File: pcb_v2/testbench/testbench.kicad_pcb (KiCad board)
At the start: 2 copper layers, 274.3 x 124.5 mm, 70 parts, among them J1 test_A, J10 test_C1, J11 test_C2, J12 test_C3, J15 lcd, J17 DEBUG, J18 power_jack, J2 test_B, J3 sub_0, J4 sub_8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

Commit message: projeto enviado para impressao em dezembro/25
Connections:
- J10 pad 1: test_0 -> test_power_vcc
- J10 pad 10: test_power_gnd_C -> test_28
- J10 pad 12: test_power_gnd_C -> test_29
- J10 pad 14: test_power_gnd_C -> test_30
- J10 pad 15: test_7 -> test_power_gnd_C
- J10 pad 4: test_power_vcc -> test_25
- J10 pad 6: test_power_vcc -> test_26
- J10 pad 8: test_power_vcc -> test_27
- J9 pad 3: unconnected-(J9-Pin_3-Pad3) -> +5V
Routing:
- net test_7: track 106.3 -> 92.8 mm
- net test_0: track 102.4 -> 88.9 mm
- net test_26: track 105.8 -> 116.7 mm
- net test_30: track 109.9 -> 120.8 mm
- net test_29: track 109.2 -> 120.1 mm
- net test_28: track 108.0 -> 119.0 mm
- net test_25: track 104.7 -> 115.7 mm
- net test_27: track 106.9 -> 117.8 mm
- net +5V: track 581.1 -> 589.7 mm
- net test_power_vcc: track 281.5 -> 276.4 mm
- net test_power_gnd_C: track 123.6 -> 125.6 mm
- net test_33: track 79.1 -> 78.0 mm
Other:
- outline, holes or cut-outs redrawn
- board text added: "ALE"
- board text added: "GND"
- board text added: "IN+"
- board text added: "IN-"
- board text added: "RX"
- board text added: "SCL"
- board text added: "SDA"
- board text added: "TX"
- board text added: "VBS"
- board text added: "VCC"

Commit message: adicionados imagens 3D para os componentes customizados
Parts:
- moved SW5 0.19 mm to (32.6, 76.2)

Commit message: versao B2 da testbench (com a alimentacao das placas de teste reposicionadas para as extremidades
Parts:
- moved R5 42.0 mm to (219.7, 51.4)
- moved R1 31.1 mm to (219.7, 47.0)
- moved R15 29.4 mm to (227.3, 129.5)
- moved R14 28.9 mm to (237.5, 129.5)
- moved R13 27.3 mm to (232.4, 129.5)
- moved R3 21.9 mm to (219.7, 42.5)
- moved D6 6.35 mm to (247.7, 135.3)
- moved D5 3.18 mm to (257.8, 135.3)
- moved R2 2.84 mm to (256.5, 51.4)
- moved R4 2.84 mm to (245.1, 51.4)
- moved R6 2.84 mm to (268.0, 51.4)
- moved Q1 2.54 mm to (250.2, 47.0)
- moved Q2 2.54 mm to (238.8, 47.0)
- moved Q3 2.54 mm to (261.6, 47.0)
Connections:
- J1 pad 1: test_0 -> test_power_vcc
- J1 pad 10: test_power_gnd_A -> test_9
- J1 pad 14: test_13 -> test_power_gnd_A
- J1 pad 15: test_24 -> test_power_vcc
- J1 pad 23: test_power_vcc -> test_32
- J1 pad 24: test_power_gnd_A -> test_33
- J1 pad 28: test_37 -> test_power_gnd_A
- J1 pad 9: test_power_vcc -> test_8
- J2 pad 1: test_0 -> test_power_vcc
- J2 pad 22: test_21 -> test_power_gnd_B
- J2 pad 23: test_24 -> test_power_vcc
- J2 pad 30: test_power_vcc -> test_31
- J2 pad 31: test_power_gnd_B -> test_32
- J2 pad 44: test_45 -> test_power_gnd_B
- J2 pad 8: test_power_vcc -> test_7
- J2 pad 9: test_power_gnd_B -> test_8
- J9 pad 5: mcu_power_scl -> mcu_power_sda
- J9 pad 6: mcu_power_sda -> mcu_power_scl
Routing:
- net test_24: track 103.5 -> 0.00 mm, vias 2 -> 0
- net test_0: track 88.9 -> 0.00 mm, vias 1 -> 0
- net mcu_power_on_C: track 116.9 -> 75.1 mm
- net test_power_vcc: track 276.4 -> 236.2 mm, vias 2 -> 0
- net Net-(D6-A): track 47.0 -> 8.41 mm
- net test_power_gnd_A: track 149.7 -> 113.9 mm
- net Net-(Q3-G): track 13.9 -> 41.2 mm
- net mcu_power_on_A: track 109.3 -> 83.3 mm
- net +5V: track 589.7 -> 610.2 mm
- net Net-(D5-A): track 45.2 -> 25.8 mm
- net Net-(Q1-G): track 13.9 -> 32.2 mm
- net test_power_gnd_B: track 120.2 -> 103.3 mm
- net test_power_gnd_C: track 125.6 -> 110.6 mm, vias 1 -> 0
- net test_21: track 145.6 -> 134.1 mm, vias 0 -> 1
- net mcu_power_on_B: track 95.6 -> 84.3 mm
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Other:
- board text added: "Rev.B1 janeiro/2026"
- board text added: "TESTBENCH"
- board text removed: "Rev.A1 dezembro/2025"
- board text removed: "TESTBENCH.A1"

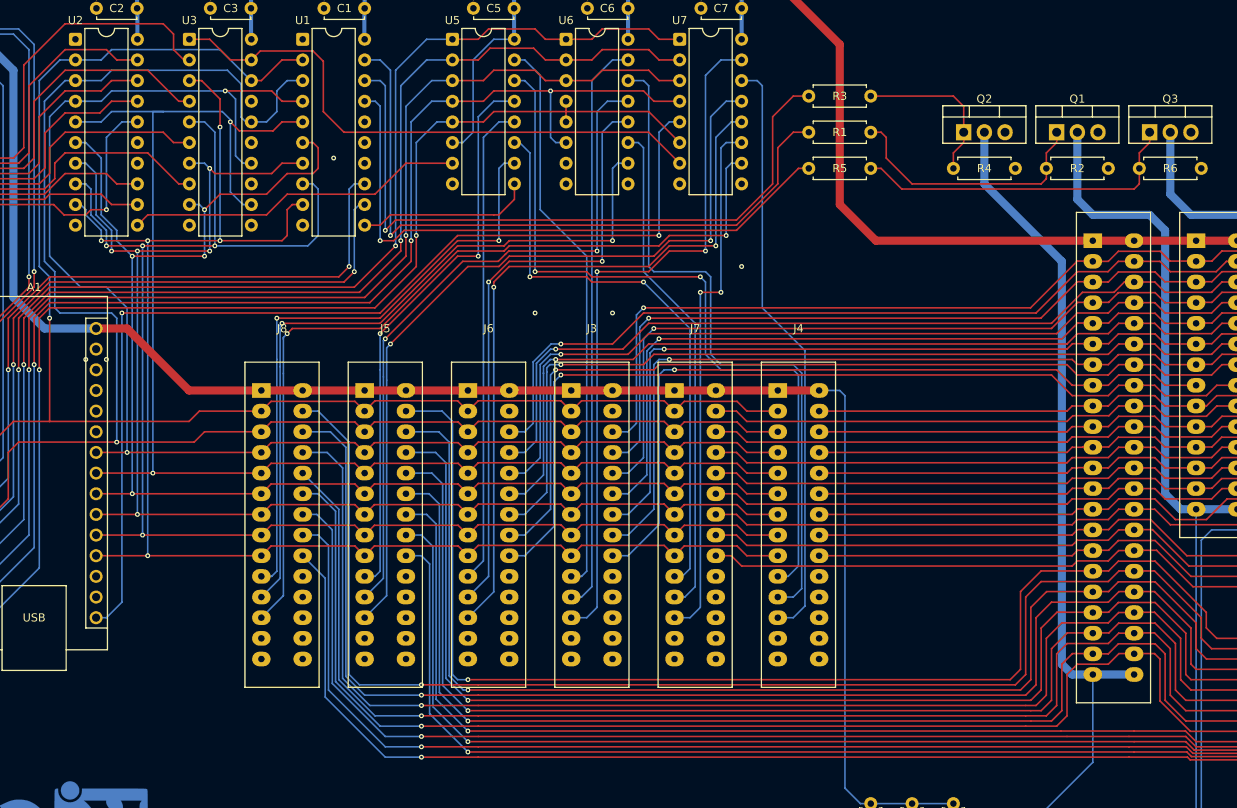
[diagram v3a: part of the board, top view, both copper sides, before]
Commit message: a interface com a sub8 parece incompativel; corrigindo a interface
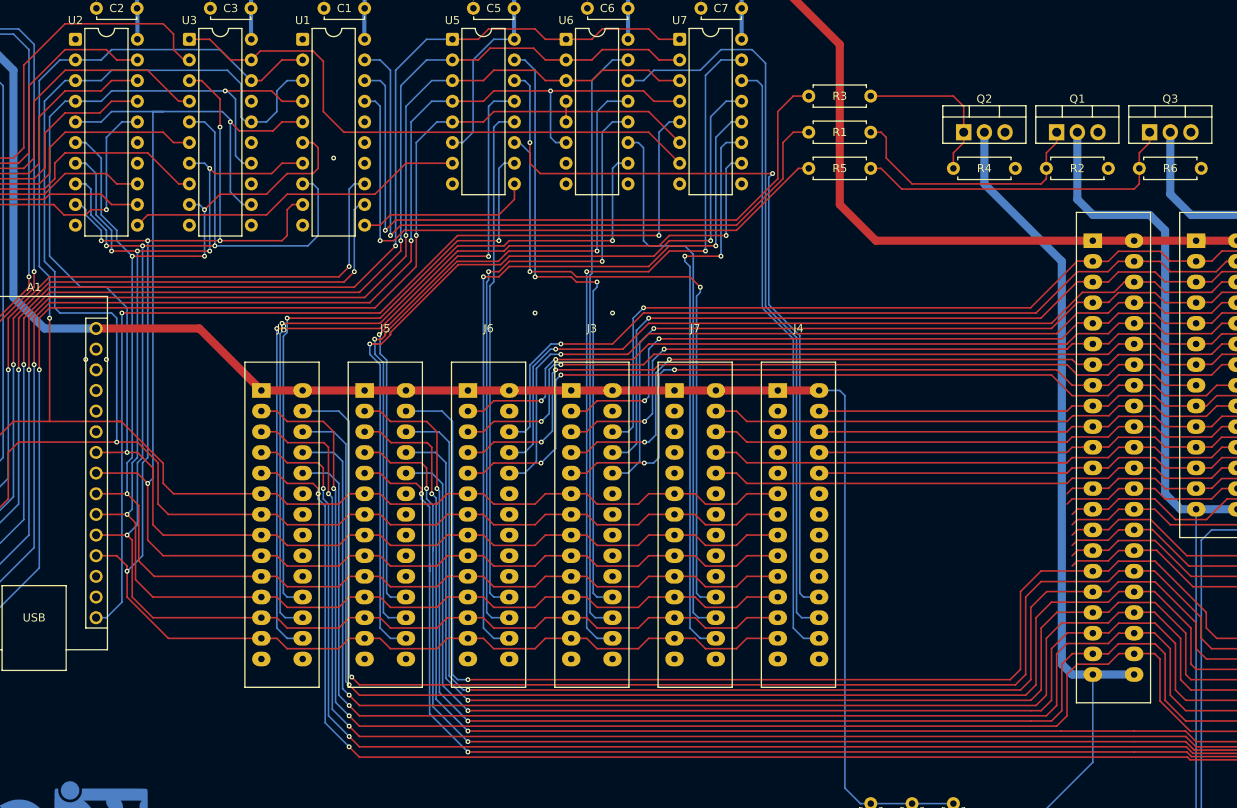
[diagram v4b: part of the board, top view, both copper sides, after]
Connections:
- J3 pad 10: write_data_0 -> mpu_data_4
- J3 pad 11: write_dir_0 -> mpu_data_5
- J3 pad 12: ~{read_enable_0} -> mpu_data_6
- J3 pad 13: unconnected-(J3-Pin_13-Pad13) -> mpu_data_7
- J3 pad 16: test_0 -> unconnected-(J3-Pin_16-Pad16)
- J3 pad 2: mpu_data_0 -> test_4
- J3 pad 20: test_4 -> unconnected-(J3-Pin_20-Pad20)
- J3 pad 21: test_5 -> unconnected-(J3-Pin_21-Pad21)
- J3 pad 22: test_6 -> unconnected-(J3-Pin_22-Pad22)
- J3 pad 23: test_7 -> unconnected-(J3-Pin_23-Pad23)
- J3 pad 25: unconnected-(J3-Pin_25-Pad25) -> write_data_0
- J3 pad 26: unconnected-(J3-Pin_26-Pad26) -> write_dir_0
- J3 pad 27: unconnected-(J3-Pin_27-Pad27) -> ~{read_enable_0}
- J3 pad 3: mpu_data_1 -> test_5
- J3 pad 4: mpu_data_2 -> test_6
- J3 pad 5: mpu_data_3 -> test_7
- J3 pad 6: mpu_data_4 -> mpu_data_0
- J3 pad 7: mpu_data_5 -> mpu_data_1
- J3 pad 8: mpu_data_6 -> mpu_data_2
- J3 pad 9: mpu_data_7 -> mpu_data_3
- J4 pad 10: write_data_8 -> mpu_data_4
- J4 pad 11: write_dir_8 -> mpu_data_5
- J4 pad 12: ~{read_enable_8} -> mpu_data_6
- J4 pad 13: unconnected-(J4-Pin_13-Pad13) -> mpu_data_7
- J4 pad 2: mpu_data_0 -> test_12
- J4 pad 20: test_12 -> unconnected-(J4-Pin_20-Pad20)
- J4 pad 21: test_13 -> unconnected-(J4-Pin_21-Pad21)
- J4 pad 22: test_14 -> unconnected-(J4-Pin_22-Pad22)
- J4 pad 23: test_15 -> unconnected-(J4-Pin_23-Pad23)
- J4 pad 25: unconnected-(J4-Pin_25-Pad25) -> write_data_8
- J4 pad 26: unconnected-(J4-Pin_26-Pad26) -> write_dir_8
- J4 pad 27: unconnected-(J4-Pin_27-Pad27) -> ~{read_enable_8}
- J4 pad 3: mpu_data_1 -> test_13
- J4 pad 4: mpu_data_2 -> test_14
- J4 pad 5: mpu_data_3 -> test_15
- J4 pad 6: mpu_data_4 -> mpu_data_0
- J4 pad 7: mpu_data_5 -> mpu_data_1
- J4 pad 8: mpu_data_6 -> mpu_data_2
- J4 pad 9: mpu_data_7 -> mpu_data_3
- J5 pad 10: write_data_16 -> mpu_data_4
- J5 pad 11: write_dir_16 -> mpu_data_5
- J5 pad 12: ~{read_enable_16} -> mpu_data_6
- J5 pad 13: unconnected-(J5-Pin_13-Pad13) -> mpu_data_7
- J5 pad 2: mpu_data_0 -> test_20
- J5 pad 20: test_20 -> unconnected-(J5-Pin_20-Pad20)
- J5 pad 21: test_21 -> unconnected-(J5-Pin_21-Pad21)
- J5 pad 22: test_22 -> unconnected-(J5-Pin_22-Pad22)
- J5 pad 23: test_23 -> unconnected-(J5-Pin_23-Pad23)
- J5 pad 25: unconnected-(J5-Pin_25-Pad25) -> write_data_16
- J5 pad 26: unconnected-(J5-Pin_26-Pad26) -> write_dir_16
- J5 pad 27: unconnected-(J5-Pin_27-Pad27) -> ~{read_enable_16}
- J5 pad 3: mpu_data_1 -> test_21
- J5 pad 4: mpu_data_2 -> test_22
- J5 pad 5: mpu_data_3 -> test_23
- J5 pad 6: mpu_data_4 -> mpu_data_0
- J5 pad 7: mpu_data_5 -> mpu_data_1
- J5 pad 8: mpu_data_6 -> mpu_data_2
- J5 pad 9: mpu_data_7 -> mpu_data_3
- J6 pad 10: write_data_24 -> mpu_data_4
- J6 pad 11: write_dir_24 -> mpu_data_5
- J6 pad 12: ~{read_enable_24} -> mpu_data_6
- J6 pad 13: unconnected-(J6-Pin_13-Pad13) -> mpu_data_7
- J6 pad 16: test_24 -> unconnected-(J6-Pin_16-Pad16)
- J6 pad 2: mpu_data_0 -> test_28
- J6 pad 20: test_28 -> unconnected-(J6-Pin_20-Pad20)
- J6 pad 21: test_29 -> unconnected-(J6-Pin_21-Pad21)
- J6 pad 22: test_30 -> unconnected-(J6-Pin_22-Pad22)
- J6 pad 23: test_31 -> unconnected-(J6-Pin_23-Pad23)
- J6 pad 25: unconnected-(J6-Pin_25-Pad25) -> write_data_24
- J6 pad 26: unconnected-(J6-Pin_26-Pad26) -> write_dir_24
- J6 pad 27: unconnected-(J6-Pin_27-Pad27) -> ~{read_enable_24}
- J6 pad 3: mpu_data_1 -> test_29
- J6 pad 4: mpu_data_2 -> test_30
- J6 pad 5: mpu_data_3 -> test_31
- J6 pad 6: mpu_data_4 -> mpu_data_0
- J6 pad 7: mpu_data_5 -> mpu_data_1
- J6 pad 8: mpu_data_6 -> mpu_data_2
- J6 pad 9: mpu_data_7 -> mpu_data_3
- J7 pad 10: write_data_32 -> mpu_data_4
- J7 pad 11: write_dir_32 -> mpu_data_5
- J7 pad 12: ~{read_enable_32} -> mpu_data_6
- J7 pad 13: unconnected-(J7-Pin_13-Pad13) -> mpu_data_7
- J7 pad 2: mpu_data_0 -> test_36
- J7 pad 20: test_36 -> unconnected-(J7-Pin_20-Pad20)
- J7 pad 21: test_37 -> unconnected-(J7-Pin_21-Pad21)
- J7 pad 22: test_38 -> unconnected-(J7-Pin_22-Pad22)
- J7 pad 23: test_39 -> unconnected-(J7-Pin_23-Pad23)
- J7 pad 25: unconnected-(J7-Pin_25-Pad25) -> write_data_32
- J7 pad 26: unconnected-(J7-Pin_26-Pad26) -> write_dir_32
- J7 pad 27: unconnected-(J7-Pin_27-Pad27) -> ~{read_enable_32}
- J7 pad 3: mpu_data_1 -> test_37
- J7 pad 4: mpu_data_2 -> test_38
- J7 pad 5: mpu_data_3 -> test_39
- J7 pad 6: mpu_data_4 -> mpu_data_0
- J7 pad 7: mpu_data_5 -> mpu_data_1
- J7 pad 8: mpu_data_6 -> mpu_data_2
- J7 pad 9: mpu_data_7 -> mpu_data_3
- J8 pad 10: write_data_40 -> mpu_data_4
- J8 pad 11: write_dir_40 -> mpu_data_5
- J8 pad 12: ~{read_enable_40} -> mpu_data_6
- J8 pad 13: unconnected-(J8-Pin_13-Pad13) -> mpu_data_7
- J8 pad 2: mpu_data_0 -> test_44
- J8 pad 20: test_44 -> unconnected-(J8-Pin_20-Pad20)
- J8 pad 21: test_45 -> unconnected-(J8-Pin_21-Pad21)
- J8 pad 22: test_46 -> unconnected-(J8-Pin_22-Pad22)
- J8 pad 23: test_47 -> unconnected-(J8-Pin_23-Pad23)
- J8 pad 25: unconnected-(J8-Pin_25-Pad25) -> write_data_40
- J8 pad 26: unconnected-(J8-Pin_26-Pad26) -> write_dir_40
- J8 pad 27: unconnected-(J8-Pin_27-Pad27) -> ~{read_enable_40}
- J8 pad 3: mpu_data_1 -> test_45
- J8 pad 4: mpu_data_2 -> test_46
- J8 pad 5: mpu_data_3 -> test_47
- J8 pad 6: mpu_data_4 -> mpu_data_0
- J8 pad 7: mpu_data_5 -> mpu_data_1
- J8 pad 8: mpu_data_6 -> mpu_data_2
- J8 pad 9: mpu_data_7 -> mpu_data_3
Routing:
- net test_38: track 78.0 -> 33.7 mm
- net test_39: track 78.0 -> 33.7 mm
- net test_37: track 78.0 -> 33.6 mm
- net test_36: track 79.1 -> 35.4 mm
- net test_15: track 61.7 -> 30.5 mm
- net test_14: track 61.7 -> 30.6 mm
- net test_13: track 63.8 -> 32.7 mm
- net test_12: track 62.7 -> 32.2 mm
- net test_47: track 146.3 -> 163.4 mm, vias 1 -> 2
- net test_45: track 148.8 -> 165.6 mm, vias 1 -> 2
- net test_44: track 163.4 -> 179.7 mm, vias 1 -> 2
- net test_46: track 148.1 -> 164.5 mm, vias 1 -> 2
- net test_23: track 132.2 -> 147.2 mm, vias 1 -> 2
- net test_22: track 133.0 -> 148.0 mm, vias 1 -> 2
- net test_21: track 134.1 -> 148.6 mm, vias 1 -> 2
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
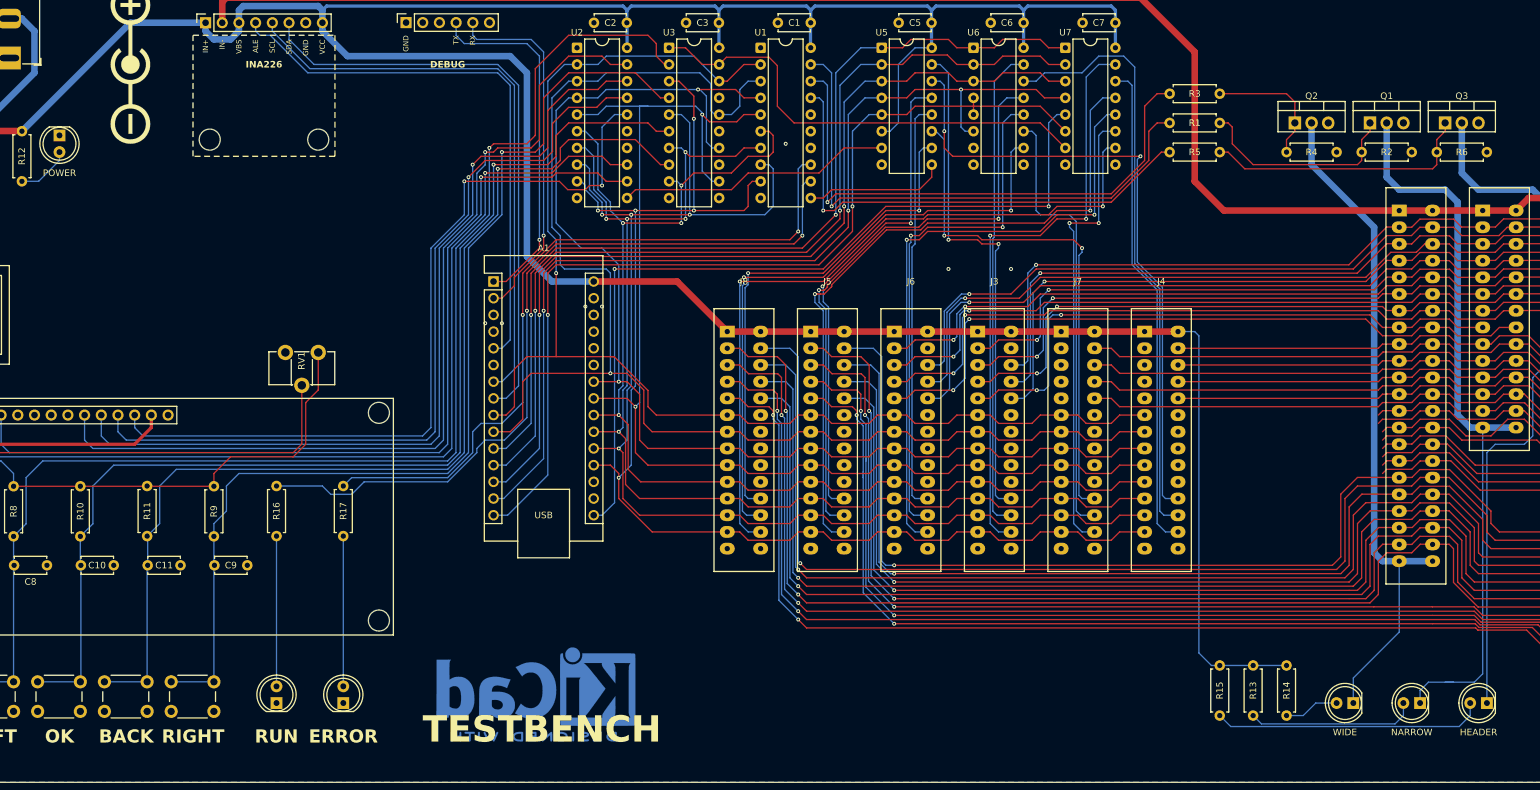
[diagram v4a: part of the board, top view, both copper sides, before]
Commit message: concluido o roteamento da revisao B1
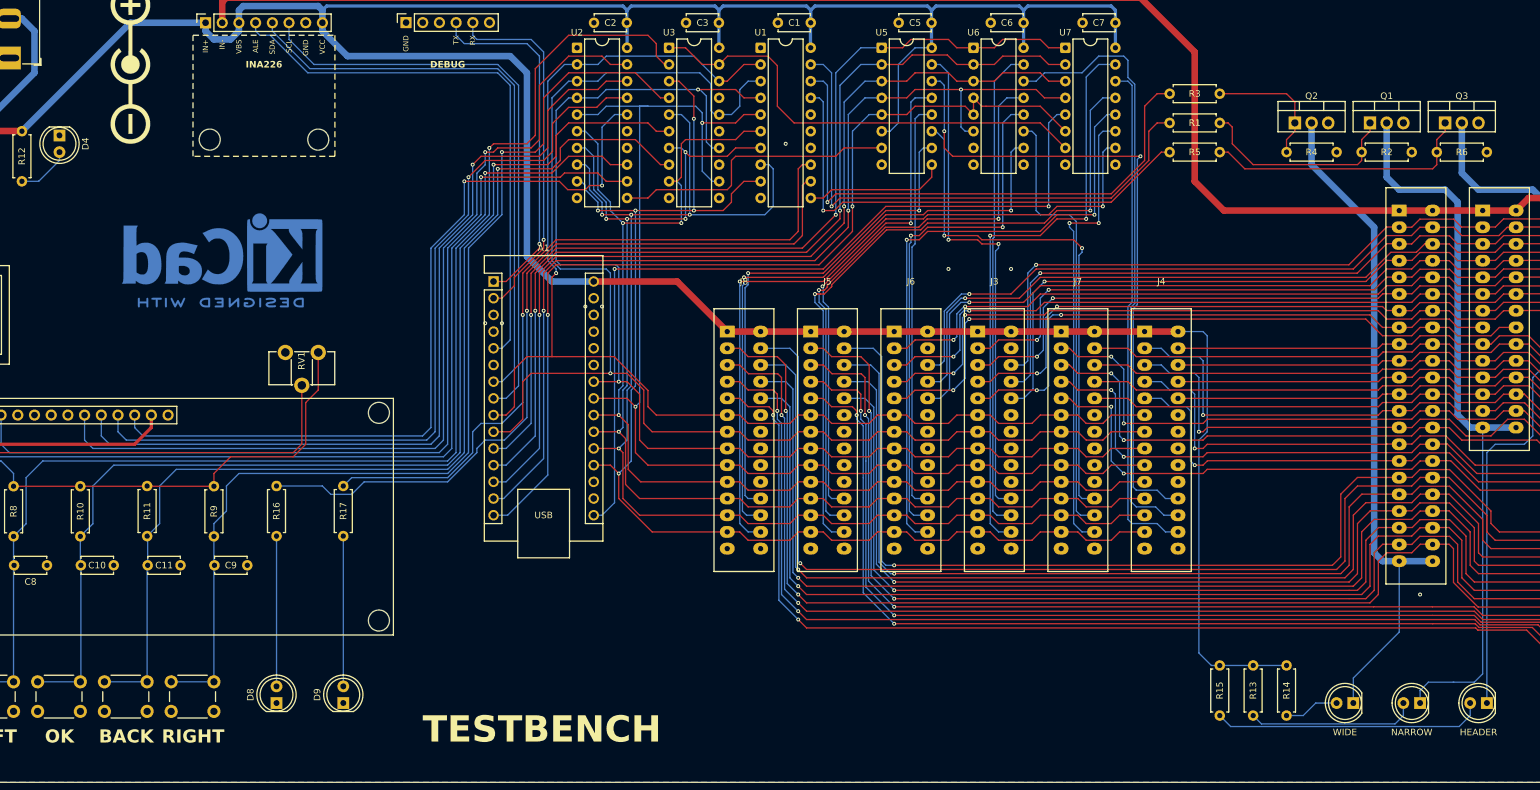
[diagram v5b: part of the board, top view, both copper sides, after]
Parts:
- moved REF** 81.4 mm to (75.6, 66.7)
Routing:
- net test_38: track 33.7 -> 92.2 mm, vias 0 -> 2
- net test_37: track 33.6 -> 92.1 mm, vias 0 -> 2
- net test_39: track 33.7 -> 92.2 mm, vias 0 -> 2
- net test_36: track 35.4 -> 93.2 mm, vias 0 -> 2
- net test_13: track 32.7 -> 77.9 mm, vias 0 -> 1
- net test_14: track 30.6 -> 75.8 mm, vias 0 -> 1
- net test_15: track 30.5 -> 75.4 mm, vias 0 -> 1
- net test_12: track 32.2 -> 76.8 mm, vias 0 -> 1
- net mpu_data_2: track 188.6 -> 191.7 mm
- net ~{read_enable_8}: track 74.8 -> 77.5 mm
- net write_data_8: track 98.0 -> 100.4 mm
- net write_dir_8: track 91.3 -> 93.6 mm
- net write_console: track 41.9 -> 44.1 mm
- net +5V: track 610.2 -> 612.0 mm
- net mpu_data_7: track 193.7 -> 192.0 mm
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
